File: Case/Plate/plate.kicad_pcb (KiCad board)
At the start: 2 copper layers, 139.1 x 77.2 mm, 1 part

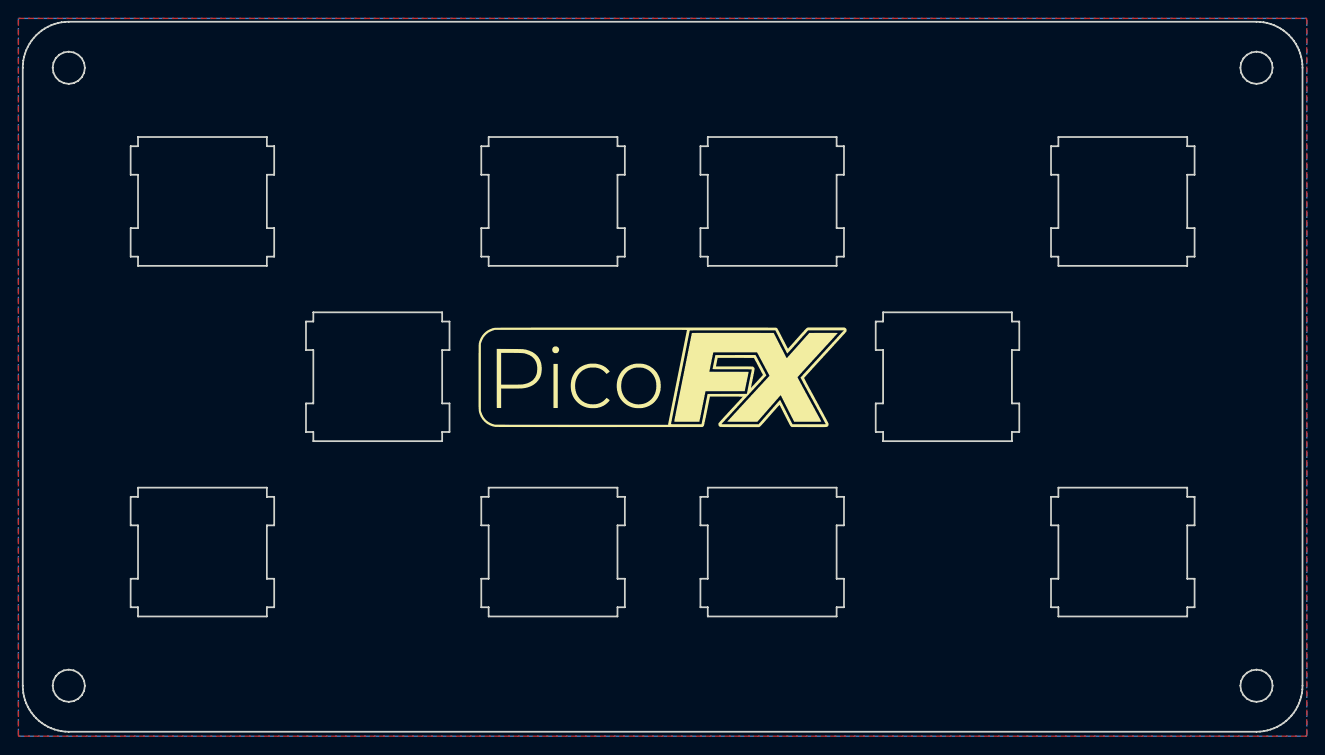
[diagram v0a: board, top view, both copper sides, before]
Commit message: Add test/service buttons to plate, begin renaming
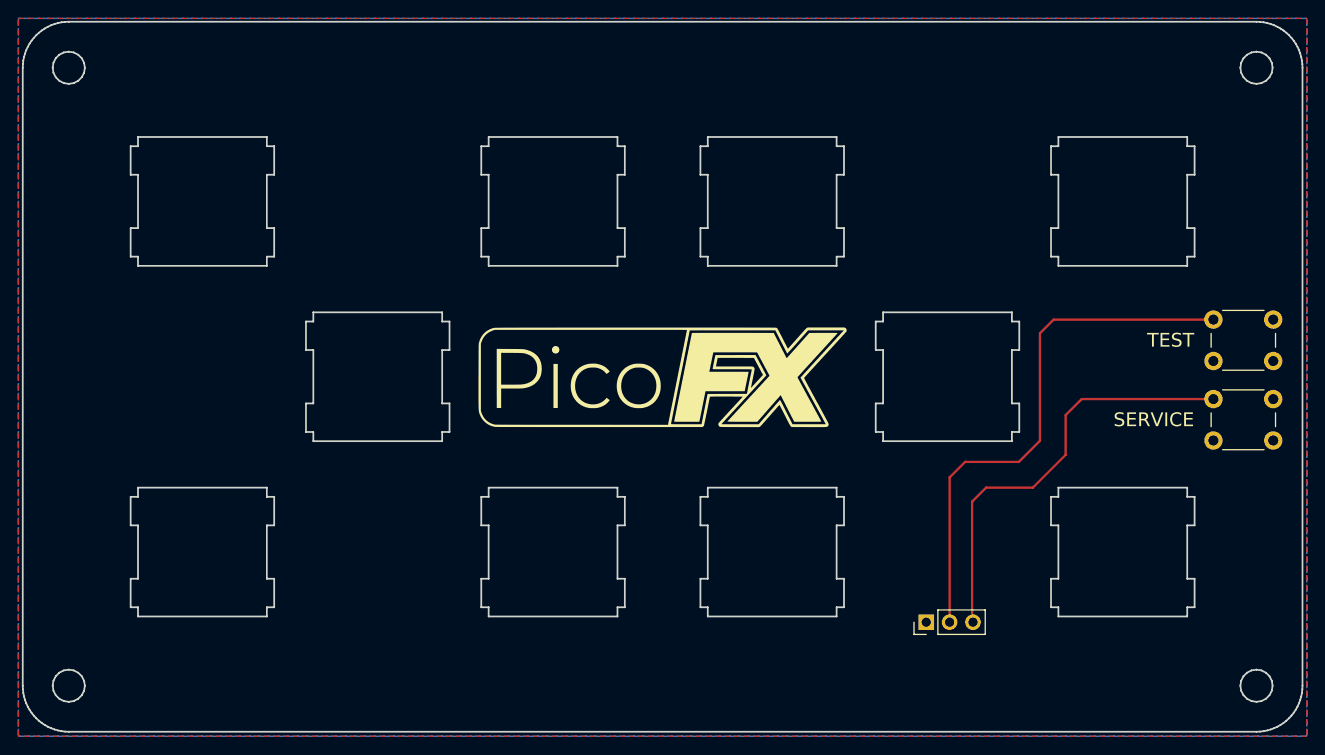
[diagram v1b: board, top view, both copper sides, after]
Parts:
- added REF**: PinHeader_1x03_P2.54mm_Vertical, Connector_PinHeader_2.54mm:PinHeader_1x03_P2.54mm_Vertical, F.Cu at (178.7, 124.6)
- added REF**: SW_PUSH_6mm_H4.3mm, Button_Switch_THT:SW_PUSH_6mm_H4.3mm, F.Cu at (209.9, 100.4)
- added REF**: SW_PUSH_6mm_H4.3mm, Button_Switch_THT:SW_PUSH_6mm_H4.3mm, F.Cu at (209.9, 91.7)
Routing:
- net TEST: track 0.00 -> 58.3 mm
- net SERVICE: track 0.00 -> 46.5 mm
- net GND: vias 0 -> 1
- added copper zone on B.Cu, net GND
- added copper zone on F.Cu, net GND
- removed copper zone on F.Cu, net (none)
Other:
- board text added: "SERVICE"
- board text added: "TEST"
